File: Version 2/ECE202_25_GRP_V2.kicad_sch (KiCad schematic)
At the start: 22 parts, among them J1 Run_in+, J2 Brake_in+, J3 Turn_in+, J4 Run_out+, J5 Brake_out+, J6 Turn_out+, J7 ground_out, J8 ground_in, J9 9v_in, K1 Running_Relay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

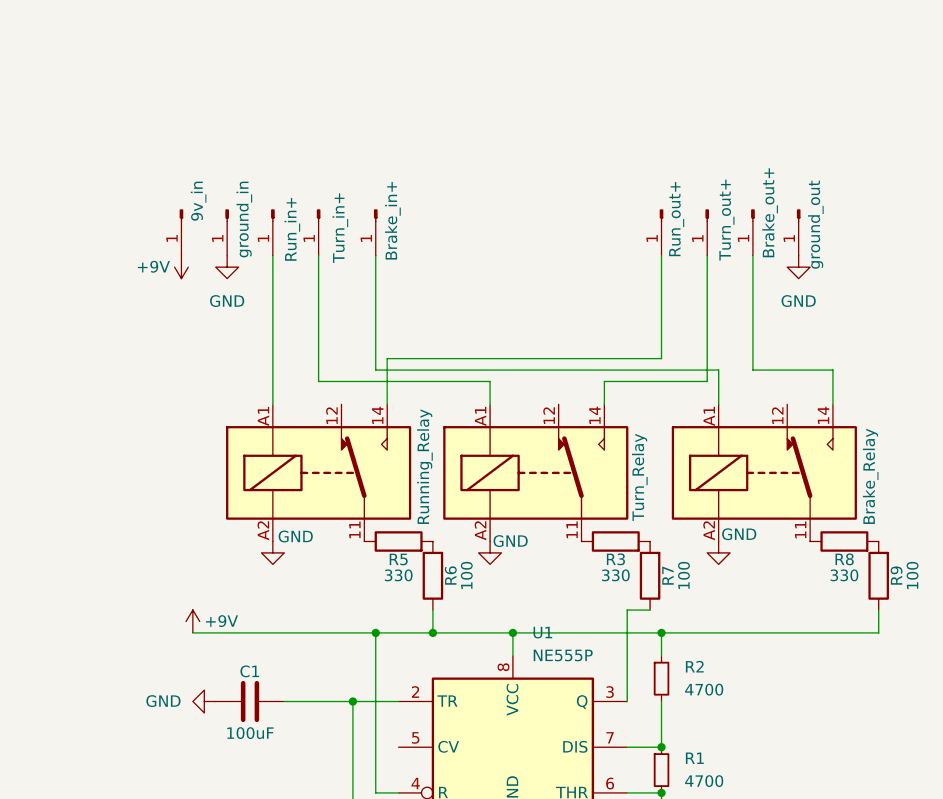
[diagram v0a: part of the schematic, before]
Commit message: V1 pcb updates, V2 pcb creation
Fixed a couple traces on V1 board, added missing ground pin. Changed pad sizes for SMD components to match on-hand inventory.

Created V2 project. Schematic done, PCB done. PCB ordered.
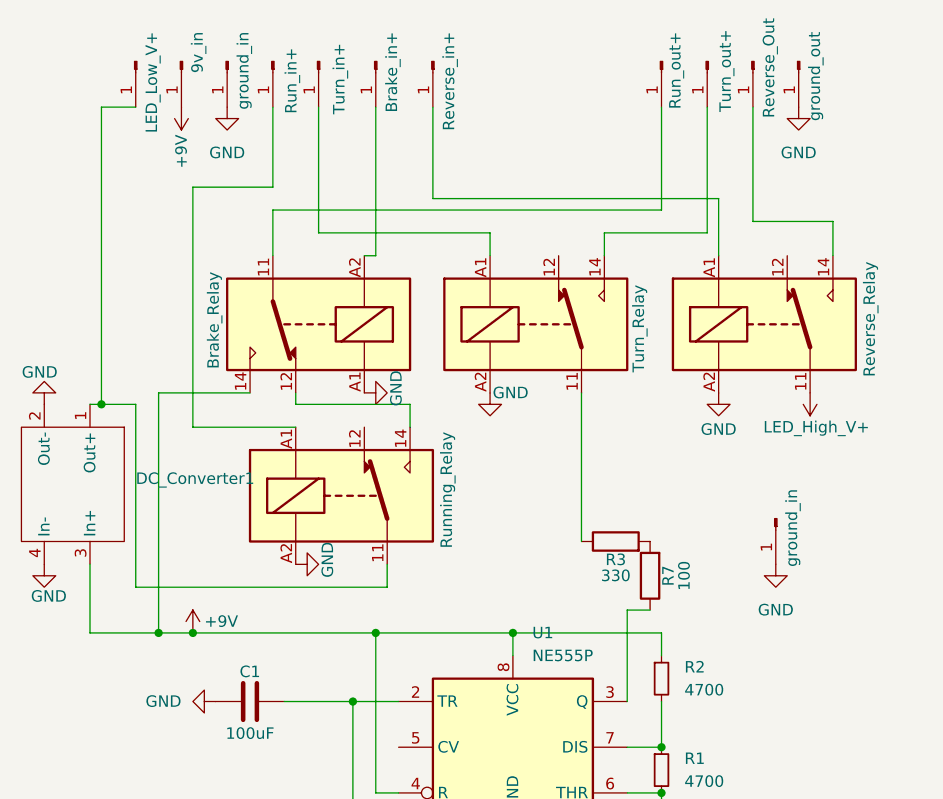
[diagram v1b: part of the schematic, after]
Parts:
- removed R5, R8: 330, Resistor_SMD:R_1206_3216Metric_Pad1.30x1.75mm_HandSolder, symbol Device:R
- removed R6, R9: 100, Resistor_SMD:R_1206_3216Metric_Pad1.30x1.75mm_HandSolder, symbol Device:R
- added DC_Converter1: ~, Converter_DCDC:MH-MINI-360, symbol Converter_DCDC:MH-MINI-360
- added J10: Reverse_in+, Connector_PinHeader_2.54mm:PinHeader_1x01_P2.54mm_Vertical, symbol Connector:Conn_01x01_Pin
- added J11: ground_in, Connector_PinHeader_2.54mm:PinHeader_1x01_P2.54mm_Vertical, symbol Connector:Conn_01x01_Pin
- added J12: LED_Low_V+, Connector_PinHeader_2.54mm:PinHeader_1x01_P2.54mm_Vertical, symbol Connector:Conn_01x01_Pin
- added K4: Running_Relay, Relay_THT:Relay_SPDT_Hongfa_JQC-3FF_0XX-1Z, symbol Relay:JQC-3FF-009-1Z
- J5: value Brake_out+ -> Reverse_Out
- K1: value Running_Relay -> Brake_Relay
- K3: value Brake_Relay -> Reverse_Relay
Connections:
- net +9V: now also K1.14, DC_Converter1.3 (In+)
- net GND: now also K1.A1, DC_Converter1.2 (Out-), DC_Converter1.4 (In-), J11.1 (Pin_1), K4.A2; no longer K1.A2
- net LED_High_V+: now reaches K3.11
- net at J2.1 (Pin_1): now also K1.A2; no longer K3.A1
- net at K1.11: now also J4.1 (Pin_1)
- net at K1.12: now also K4.14
- net at J1.1 (Pin_1): now also K4.A1; no longer K1.A1
- new net: DC_Converter1.1 (Out+), J12.1 (Pin_1), K4.11
- new net: J10.1 (Pin_1), K3.A1

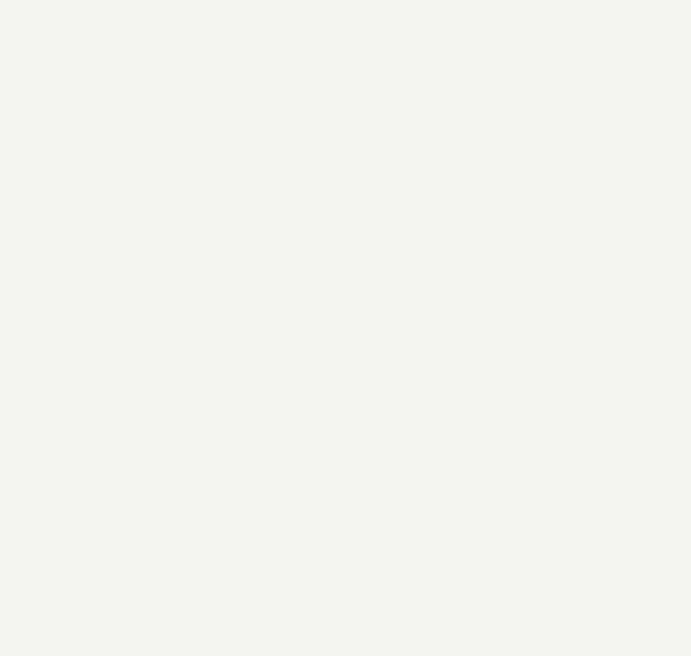
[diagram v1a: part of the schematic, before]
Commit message: LED Board, practice board, button board updates
Created led board and practice board/business card. Updated mounting for buttons on button board. Submitted all 3 for production on 4/6/25
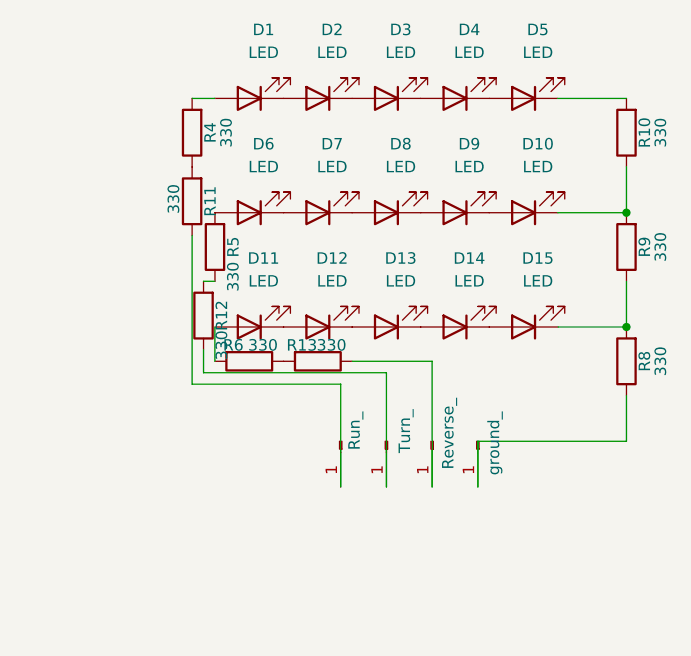
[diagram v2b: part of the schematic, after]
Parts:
- added D1, D10, D11, D12, D13, D14, D15, D2, D3, D4, D5, D6, D7, D8, D9: LED, LED_SMD:LED_1206_3216Metric_Pad1.42x1.75mm_HandSolder, symbol Device:LED
- added J13: Run_, Connector_PinHeader_2.54mm:PinHeader_1x01_P2.54mm_Vertical, symbol Connector:Conn_01x01_Pin
- added J14: Turn_, Connector_PinHeader_2.54mm:PinHeader_1x01_P2.54mm_Vertical, symbol Connector:Conn_01x01_Pin
- added J15: Reverse_, Connector_PinHeader_2.54mm:PinHeader_1x01_P2.54mm_Vertical, symbol Connector:Conn_01x01_Pin
- added J16: ground_, Connector_PinHeader_2.54mm:PinHeader_1x01_P2.54mm_Vertical, symbol Connector:Conn_01x01_Pin
- added R10, R11, R12, R13, R4, R5, R6, R8, R9: 330, Resistor_SMD:R_1206_3216Metric_Pad1.30x1.75mm_HandSolder, symbol Device:R
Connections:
- new net: J13.1 (Pin_1), R11.1
- new net: R11.2, R4.1
- new net: D4.1 (K), D5.2 (A)
- new net: D3.1 (K), D4.2 (A)
- new net: D2.1 (K), D3.2 (A)
- new net: D1.1 (K), D2.2 (A)
- new net: D15.1 (K), R8.2, R9.1
- new net: D14.1 (K), D15.2 (A)
- new net: D11.1 (K), D12.2 (A)
- new net: D11.2 (A), R6.2
- new net: R12.2, R5.1
- new net: D6.2 (A), R5.2
- new net: D8.1 (K), D9.2 (A)
- new net: D7.1 (K), D8.2 (A)
- new net: R13.2, R6.1
- new net: J16.1 (Pin_1), R8.1
- new net: D10.2 (A), D9.1 (K)
- new net: J14.1 (Pin_1), R12.1
- new net: D13.1 (K), D14.2 (A)
- new net: D12.1 (K), D13.2 (A)
- new net: D5.1 (K), R10.2
- new net: D6.1 (K), D7.2 (A)
- new net: D10.1 (K), R10.1, R9.2
- new net: D1.2 (A), R4.2
- new net: J15.1 (Pin_1), R13.1
